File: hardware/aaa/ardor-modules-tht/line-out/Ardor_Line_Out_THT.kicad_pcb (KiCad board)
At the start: 2 copper layers, 115 x 85 mm, 29 parts, among them J101 5V POWER + ENABLE INPUT, J102 MONO AUDIO INPUT FROM SOURCE, J502 AUDIO OUTPUT TO AMP INPUT, J503 LINE AUDIO OUTPUT TO TS SOCKET, K501 Omron G5V-1 DC5, Q501 2N3904 / E-B-C, U501 MCP6022-I/P

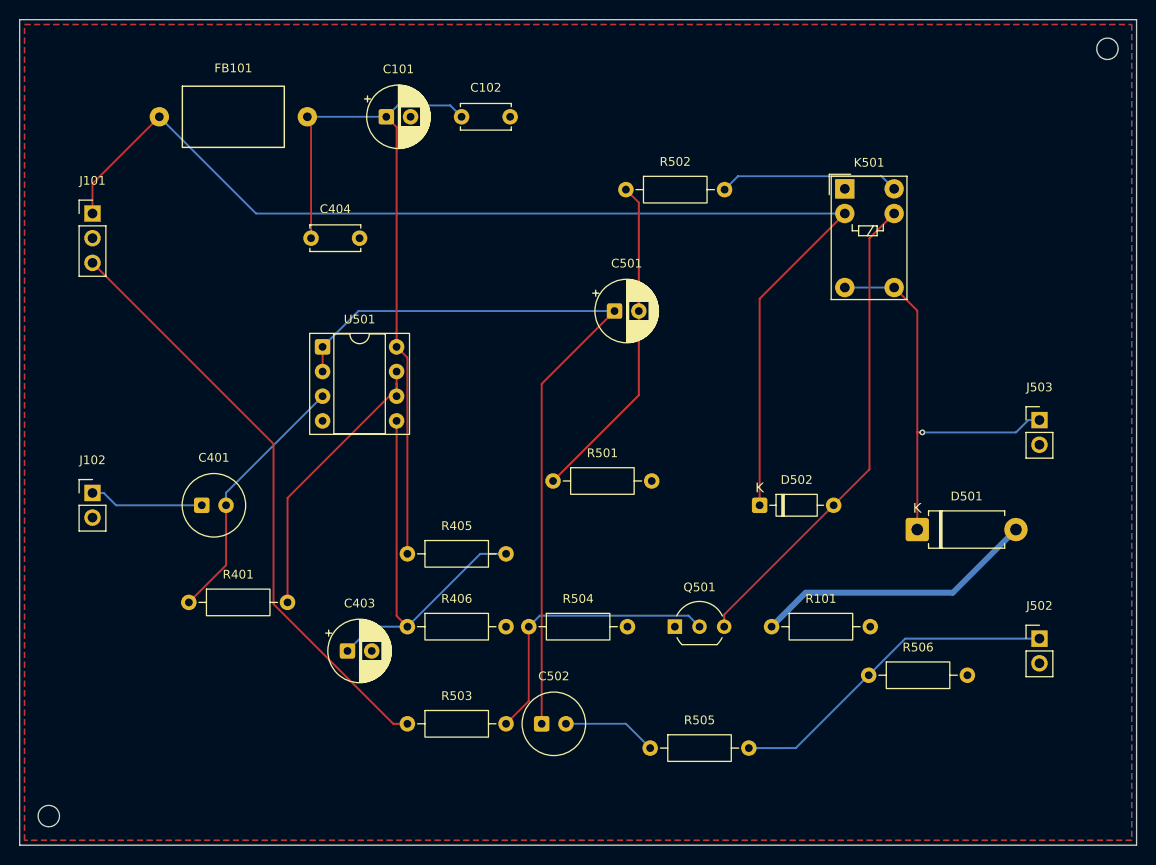
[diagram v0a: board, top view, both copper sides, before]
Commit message: fix(hardware): use Hestore TVS diodes in hand-assembly modules
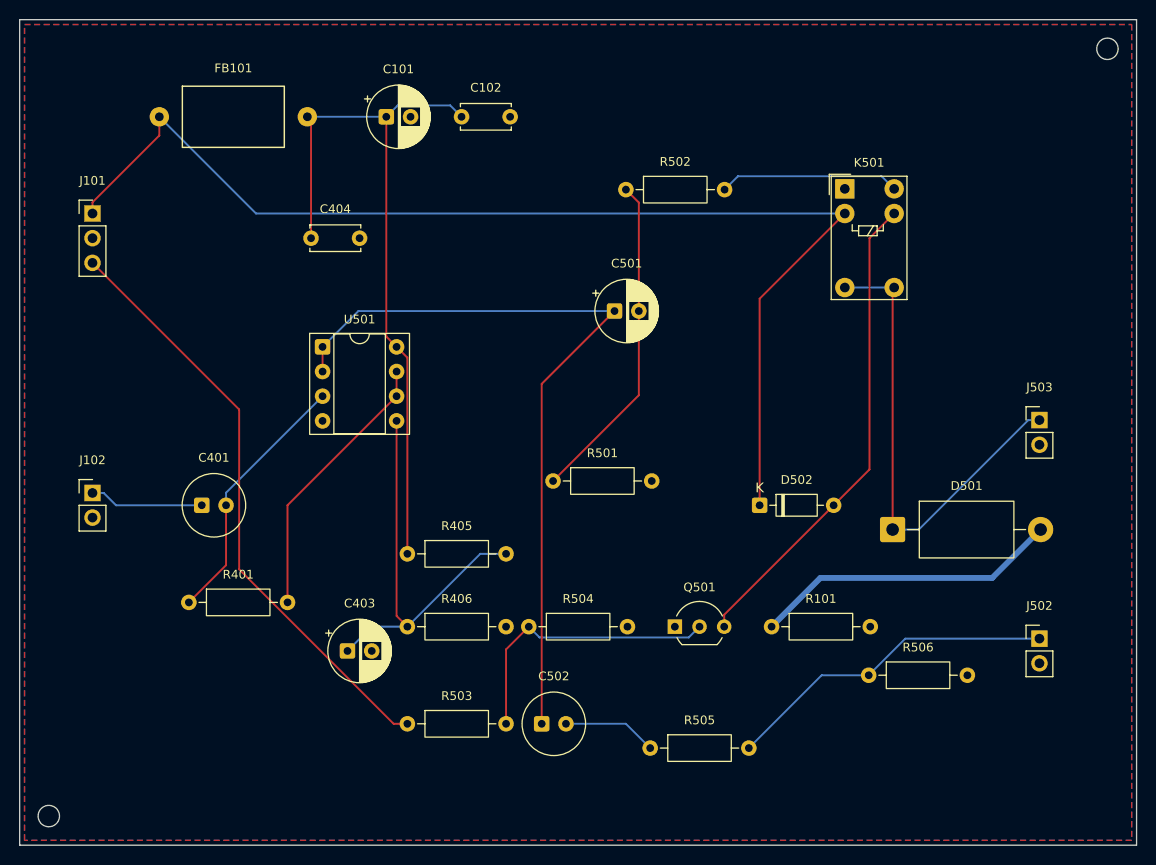
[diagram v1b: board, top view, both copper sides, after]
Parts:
- D501: value SA5.0CA-E3/54 -> 1.5KE6.8CA; footprint Diode_THT:D_DO-15_P10.16mm_Horizontal -> Ardor_THT:D_TVS_DC_1.5KE_P15.24mm
- moved D501 2.54 mm to (139.9, 102.5)
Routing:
- net Net-(D501-A1): track 44.1 -> 49.9 mm, vias 1 -> 0
- net /CHASSIS: track 29.3 -> 31.8 mm
- net /VREF: track 29.7 -> 28.4 mm

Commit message: feat(hardware): compact layouts and adopt Hestore module packages
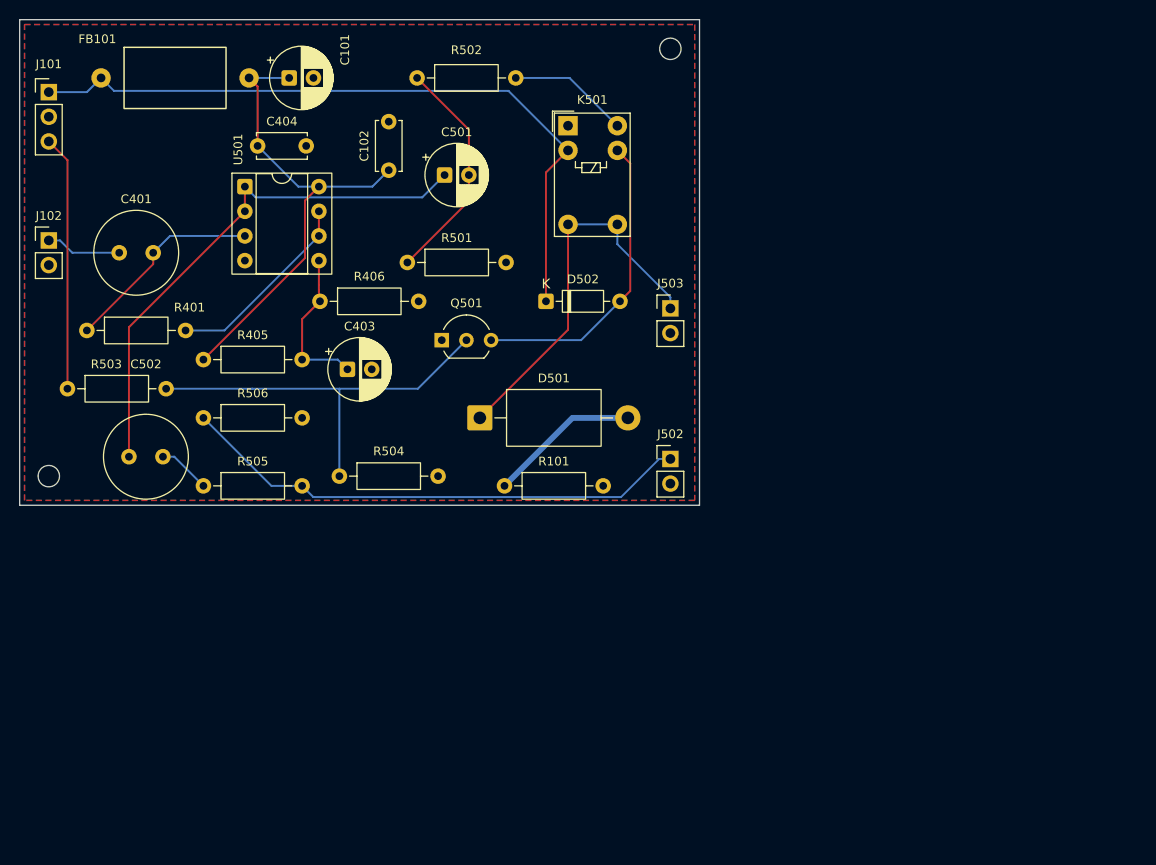
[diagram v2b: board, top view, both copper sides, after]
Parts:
- C401, C502: value 10u / 25V BIPOLAR -> 10u / 50V BIPOLAR; footprint Ardor_THT:CP_Bipolar_D6.3mm_P2.50mm -> Ardor_THT:CP_Bipolar_Nichicon_D8.0mm_P3.50mm
- moved R506 73.4 mm to (68.9, 91.0)
- moved R505 53.3 mm to (68.9, 98.0)
- moved C502 50.6 mm to (61.2, 95.0)
- moved R503 49.1 mm to (54.9, 88.0)
- moved H2 45.0 mm to (117.0, 53.0)
- moved D501 44.0 mm to (97.4, 91.0)
- moved J502 42.3 mm to (117.0, 95.2)
- moved J503 39.7 mm to (117.0, 79.7)
- moved Q501 38.0 mm to (93.5, 83.0)
- moved H1 35.0 mm to (53.0, 97.0)
- moved R406 34.7 mm to (80.9, 79.0)
- moved R101 31.1 mm to (99.9, 98.0)
- moved D502 30.4 mm to (104.2, 79.0)
- moved R401 29.9 mm to (56.9, 82.0)
- moved K501 29.2 mm to (106.5, 60.9)
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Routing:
- net /+5V: track 121.2 -> 73.6 mm
- net Net-(J101-Pin_3): track 61.7 -> 26.3 mm
- net Net-(U501B-+): track 42.1 -> 16.1 mm
- net /+5V_A: track 75.4 -> 50.2 mm
- net Net-(U501A--): track 79.7 -> 54.7 mm
- net Net-(J502-Pin_1): track 34.6 -> 53.1 mm
- net Net-(D502-A): track 49.8 -> 31.5 mm
- net /CHASSIS: track 31.8 -> 15.6 mm
- net Net-(Q501-B): track 29.5 -> 42.0 mm
- net Net-(C501-Pad2): track 34.2 -> 23.8 mm
- net Net-(D501-A1): track 49.9 -> 39.7 mm
- net /VREF: track 28.4 -> 20.3 mm
- net Net-(K501-Pad10): track 18.6 -> 12.5 mm
- net Net-(U501A-+): track 26.9 -> 21.0 mm
- net Net-(C502-Pad2): track 9.71 -> 5.41 mm
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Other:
- board size 115 x 85 mm -> 70 x 50 mm
